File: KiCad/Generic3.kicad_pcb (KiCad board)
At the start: 2 copper layers, 35 x 21.5 mm, 35 parts, among them J1 DC, J2 I/O, J3 USB-C, U1 ESP32-PICO-MINI-02, U2 LMR16006+FB, U3 FT231XQ, U4 QR

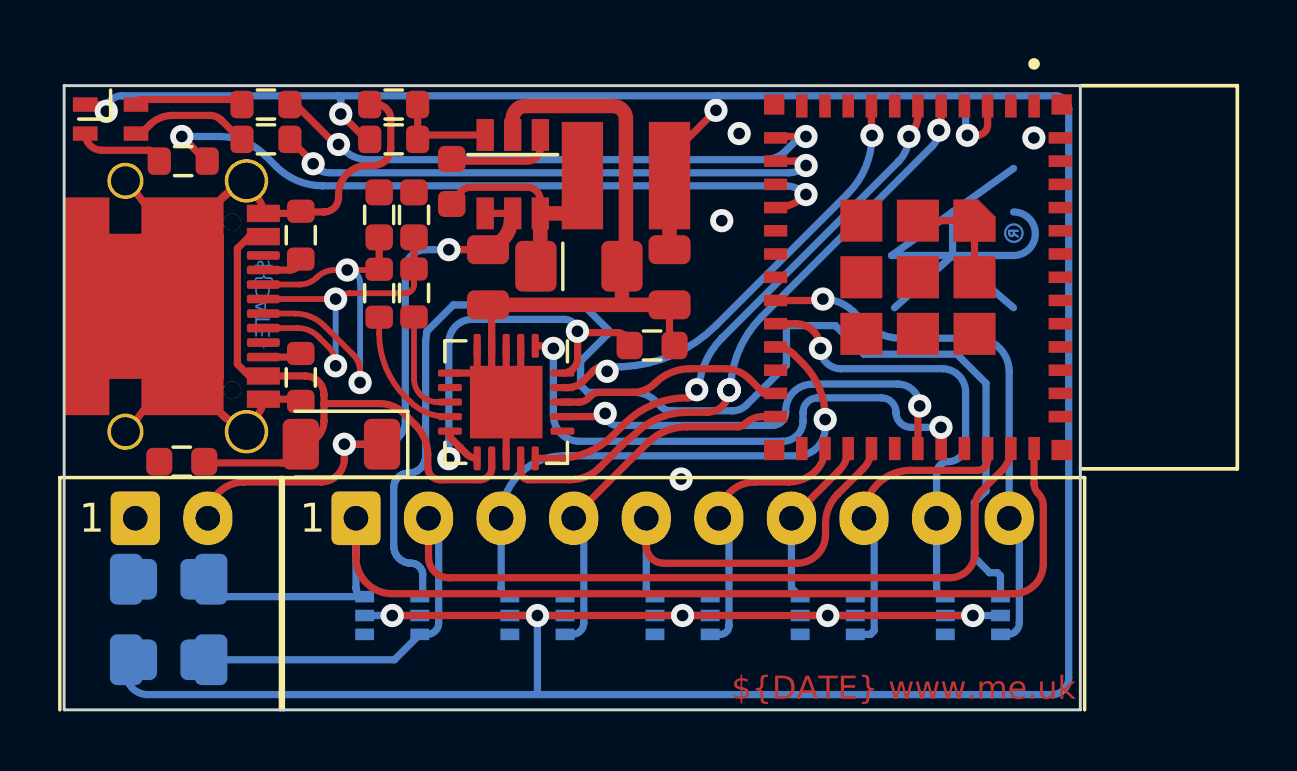
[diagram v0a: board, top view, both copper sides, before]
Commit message: Tidy GPIO usage
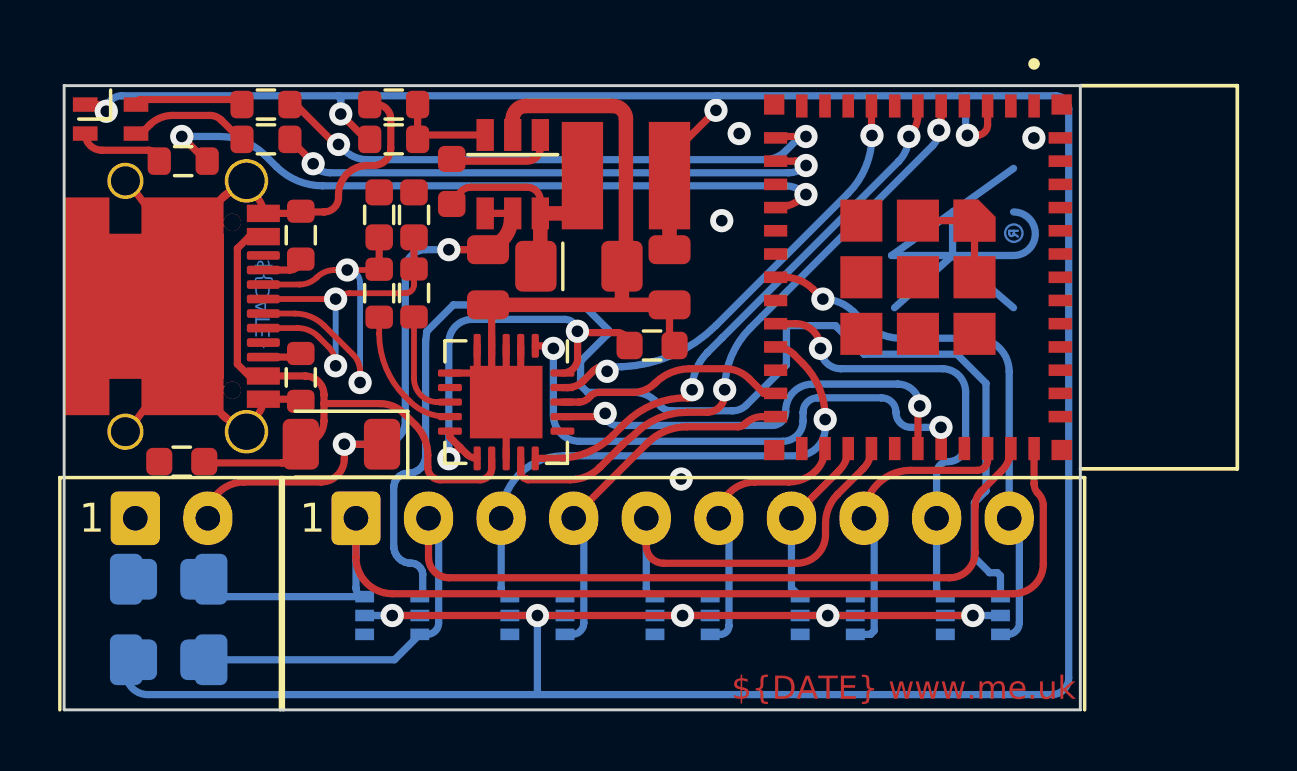
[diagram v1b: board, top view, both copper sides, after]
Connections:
- U1 pad 18: unconnected-(U1-Pad18) -> IO10
- U1 pad 19: IO10 -> unconnected-(U1-Pad19)
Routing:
- net CHARGER: vias 4 -> 2
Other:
- board text added: "14"
- board text removed: "12"
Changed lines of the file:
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@@
   (net 27 "CHARGER")
   (net 28 "USB")
-  (net 29 "unconnected-(U1-Pad18)")
+  (net 29 "unconnected-(U1-Pad19)")
   (net 30 "unconnected-(U1-Pad22)")
   (net 31 "GPIO0")
@@
       (primitives
     (gr_arc (start 2.89 -3.045) (mid 0 -0.155) (end -2.89 -3.045) (width 0.25))
-    (gr_arc (start 4.294753 -3.49127) (mid -0.020907 -1.02625) (end -4.315692 -3.527464) (width 0.25))
+    (gr_arc (start 4.294753 -3.49127) (mid -0.016568 -1.026234) (end -4.311371 -3.519937) (width 0.25))
     (gr_arc (start -3.2 -2.485) (mid -4.015 -3.3) (end -3.2 -4.115) (width 0.25))
     (gr_arc (start 3.2 -4.115) (mid 4.015 -3.3) (end 3.2 -2.485) (width 0.25))
-    (gr_arc (start -4.32 0.635) (mid 0 -1.154403) (end 4.32 0.635) (width 0.25))
+    (gr_arc (start -4.32 0.635) (mid -0.000001 -1.154403) (end 4.319999 0.634999) (width 0.25))
         (gr_poly (pts
             (xy -3.75 -2.745)
@@
       (net 44 "unconnected-(U1-Pad17)") (pinfunction "IO27") (pintype "bidirectional+no_connect"))
     (pad "18" smd rect (at 0 4.9 270) (size 0.4 0.8) (layers "F.Cu" "F.Paste" "F.Mask")
-      (net 29 "unconnected-(U1-Pad18)") (pinfunction "IO14") (pintype "bidirectional+no_connect"))
+      (net 14 "IO10") (pinfunction "IO14") (pintype "bidirectional"))
     (pad "19" smd rect (at 0.8 4.9 270) (size 0.4 0.8) (layers "F.Cu" "F.Paste" "F.Mask")
-      (net 14 "IO10") (pinfunction "IO12") (pintype "bidirectional"))
+      (net 29 "unconnected-(U1-Pad19)") (pinfunction "IO12") (pintype "bidirectional+no_connect"))
     (pad "20" smd rect (at 1.6 4.9 270) (size 0.4 0.8) (layers "F.Cu" "F.Paste" "F.Mask")
       (net 12 "IO9") (pinfunction "IO13") (pintype "bidirectional"))
@@
     (effects (font (size 1 1) (thickness 0.15)) (justify mirror))
   )
-  (gr_text "12" (at 169.5 74.75) (layer "B.SilkS")
+  (gr_text "14" (at 169.5 74.75) (layer "B.SilkS")
     (effects (font (size 1 1) (thickness 0.15)) (justify mirror))
   )
@@
   (arc (start 147.9 66.6) (mid 148.465685 66.365685) (end 148.7 65.8) (width 0.25) (layer "B.Cu") (net 13))
   (arc (start 148.7 60.6) (mid 148.905025 60.105025) (end 149.4 59.9) (width 0.25) (layer "B.Cu") (net 13))
-  (segment (start 161.45675 61.65) (end 162.963875 61.65) (width 0.25) (layer "F.Cu") (net 14))
+  (segment (start 162.741031 61.258969) (end 163.082801 61.600739) (width 0.25) (layer "F.Cu") (net 14))
+  (segment (start 161.45675 60.85) (end 161.753693 60.85) (width 0.25) (layer "F.Cu") (net 14))
   (via (at 163.082801 61.600739) (size 0.8) (drill 0.4) (layers "F.Cu" "B.Cu") (net 14))
-  (arc (start 162.963875 61.65) (mid 163.028237 61.637197) (end 163.082801 61.600739) (width 0.25) (layer "F.Cu") (net 14))
+  (arc (start 161.753693 60.85) (mid 162.288036 60.956288) (end 162.741031 61.258969) (width 0.25) (layer "F.Cu") (net 14))
   (segment (start 165.75 62.95) (end 168.35 62.95) (width 0.25) (layer "B.Cu") (net 14))
   (segment (start 169.5 64.1) (end 169.5 69.15) (width 0.25) (layer "B.Cu") (net 14))
@@
   (segment (start 167.096281 55.765112) (end 167.077425 55.783968) (width 0.25) (layer "F.Cu") (net 27))
   (segment (start 167.15675 54.95) (end 167.15675 55.628909) (width 0.25) (layer "F.Cu") (net 27))
+  (segment (start 159.7 64.724501) (end 159.7 64.895909) (width 0.25) (layer "F.Cu") (net 27))
   (segment (start 152.92452 67.82452) (end 154.375119 67.82452) (width 0.25) (layer "F.Cu") (net 27))
   (via (at 167.077425 55.783968) (size 0.8) (drill 0.4) (layers "F.Cu" "B.Cu") (net 27))
-  (via (at 159.848254 64.747655) (size 0.8) (drill 0.4) (layers "F.Cu" "B.Cu") (net 27))
-  (via (at 159.848254 64.747655) (size 0.8) (drill 0.4) (layers "F.Cu" "B.Cu") (net 27))
-  (via (at 159.858917 64.724501) (size 0.8) (drill 0.4) (layers "F.Cu" "B.Cu") (net 27))
-  (arc (start 159.095909 65.5) (mid 159.627897 65.279643) (end 159.848254 64.747655) (width 0.25) (layer "F.Cu") (net 27))
+  (via (at 159.7 64.724501) (size 0.8) (drill 0.4) (layers "F.Cu" "B.Cu") (net 27))
   (arc (start 156.180761 66.619239) (mid 156.375762 66.441302) (end 156.582369 66.276767) (width 0.25) (layer "F.Cu") (net 27))
+  (arc (start 159.7 64.895909) (mid 159.523066 65.323066) (end 159.095909 65.5) (width 0.25) (layer "F.Cu") (net 27))
   (arc (start 152.675 67.575) (mid 152.740901 67.734099) (end 152.9 67.8) (width 0.25) (layer "F.Cu") (net 27))
   (arc (start 154.375119 67.82452) (mid 154.929781 67.714191) (end 155.4 67.4) (width 0.25) (layer "F.Cu") (net 27))
   (arc (start 167.15675 55.628909) (mid 167.140248 55.694791) (end 167.096281 55.747573) (width 0.25) (layer "F.Cu") (net 27))
   (arc (start 156.623134 66.236002) (mid 157.438367 65.691281) (end 158.4 65.5) (width 0.25) (layer "F.Cu") (net 27))
-  (segment (start 159.937296 64.646122) (end 159.858917 64.724501) (width 0.25) (layer "B.Cu") (net 27))
   (segment (start 166.849668 56.333822) (end 160.972335 62.211156) (width 0.25) (layer "B.Cu") (net 27))
-  (segment (start 159.937296 64.262448) (end 159.937296 64.646122) (width 0.25) (layer "B.Cu") (net 27))
-  (arc (start 160.972335 62.211156) (mid 160.290925 63.153893) (end 159.937296 64.262448) (width 0.25) (layer "B.Cu") (net 27))
+  (segment (start 160.577527 62.605965) (end 160.972335 62.211156) (width 0.25) (layer "B.Cu") (net 27))
+  (arc (start 159.7 64.724501) (mid 159.928062 63.577957) (end 160.577527 62.605965) (width 0.25) (layer "B.Cu") (net 27))
   (arc (start 167.077425 55.783968) (mid 167.018233 56.081547) (end 166.849668 56.333822) (width 0.25) (layer "B.Cu") (net 27))
   (segment (start 156.262715 65.885293) (end 156.133426 66.014581) (width 0.25) (layer "F.Cu") (net 28))
   (segment (start 156.133426 66.014581) (end 155.848505 66.299502) (width 0.25) (layer "F.Cu") (net 28))
   (segment (start 166.35675 54.95) (end 166.35675 55.246475) (width 0.25) (layer "F.Cu") (net 28))
+  (segment (start 158.578424 64.7245) (end 158.578424 64.821576) (width 0.25) (layer "F.Cu") (net 28))
   (segment (start 153.94611 67.0875) (end 153.175 67.0875) (width 0.25) (layer "F.Cu") (net 28))
   (segment (start 158.461841 65) (end 158.4 65) (width 0.25) (layer "F.Cu") (net 28))
-  (via (at 158.737341 64.7245) (size 0.8) (drill 0.4) (layers "F.Cu" "B.Cu") (net 28))
+  (via (at 158.578424 64.7245) (size 0.8) (drill 0.4) (layers "F.Cu" "B.Cu") (net 28))
   (via (at 166.044629 56.000001) (size 0.8) (drill 0.4) (layers "F.Cu" "B.Cu") (net 28))
+  (arc (start 158.578424 64.821576) (mid 158.526165 64.947741) (end 158.4 65) (width 0.25) (layer "F.Cu") (net 28))
   (arc (start 155.848505 66.299502) (mid 154.975679 66.882706) (end 153.94611 67.0875) (width 0.25) (layer "F.Cu") (net 28))
   (arc (start 158.737341 64.7245) (mid 158.656649 64.919308) (end 158.461841 65) (width 0.25) (layer "F.Cu") (net 28))
   (arc (start 158.4 65) (mid 157.243309 65.23008) (end 156.262715 65.885293) (width 0.25) (layer "F.Cu") (net 28))
   (arc (start 166.35675 55.246475) (mid 166.275632 55.65428) (end 166.044629 56.000001) (width 0.25) (layer "F.Cu") (net 28))
-  (segment (start 158.836962 64.43365) (end 158.836962 64.624879) (width 0.25) (layer "B.Cu") (net 28))
-  (segment (start 158.836962 64.624879) (end 158.737341 64.7245) (width 0.25) (layer "B.Cu") (net 28))
   (segment (start 165.688847 56.858935) (end 159.614741 62.933041) (width 0.25) (layer "B.Cu") (net 28))
+  (segment (start 159.11239 63.435392) (end 159.614741 62.933041) (width 0.25) (layer "B.Cu") (net 28))
   (arc (start 166.044629 56.000001) (mid 165.952164 56.464853) (end 165.688847 56.858935) (width 0.25) (layer "B.Cu") (net 28))
-  (arc (start 159.614741 62.933041) (mid 159.11031 63.62325) (end 158.836962 64.43365) (width 0.25) (layer "B.Cu") (net 28))
+  (arc (start 158.578424 64.7245) (mid 158.717197 64.02684) (end 159.11239 63.435392) (width 0.25) (layer "B.Cu") (net 28))
   (segment (start 161.051934 64.85) (end 161.45675 64.85) (width 0.25) (layer "F.Cu") (net 31))
   (segment (start 160.550967 64.349033) (end 161.051934 64.85) (width 0.25) (layer "F.Cu") (net 31))

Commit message: Fixed USB/DC stuff on Generic.
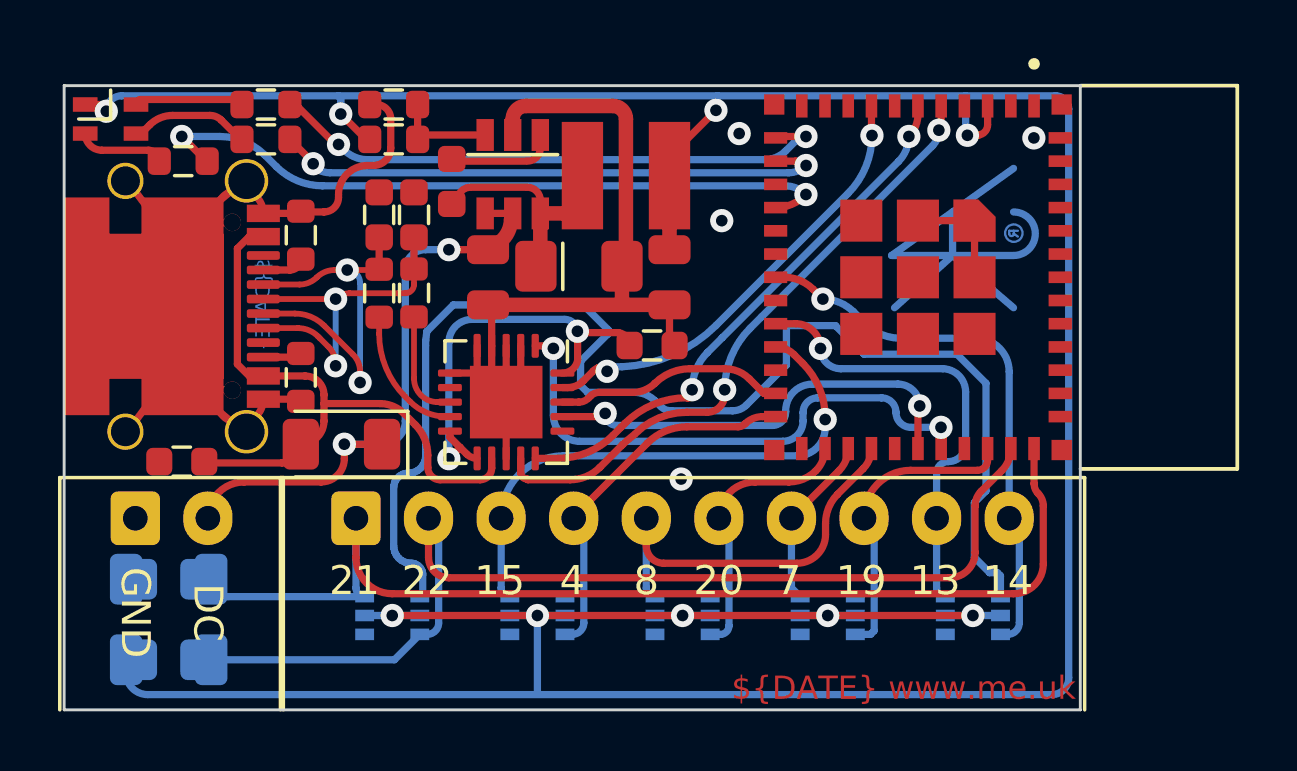
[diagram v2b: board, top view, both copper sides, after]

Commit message: Generic3 VBUS tidy
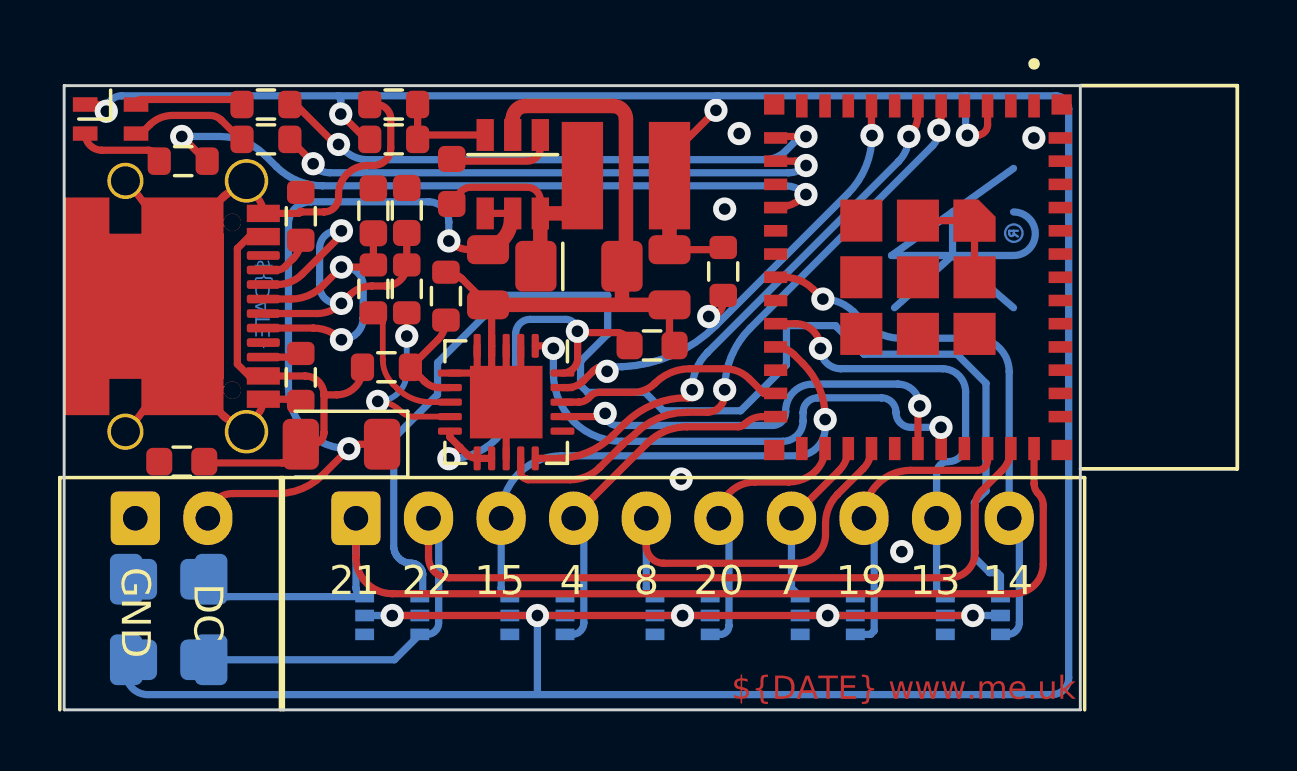
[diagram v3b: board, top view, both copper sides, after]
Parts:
- added R1: 10k, RevK:R_0603, F.Cu at (159.7, 60.6)
- added R11: 4k7, RevK:R_0603, F.Cu at (148.1, 64.0)
- added R12: 10k, RevK:R_0603, F.Cu at (150.1, 61.5)
- moved C3 1.41 mm to (147.6, 58.6)
- moved R8 1.41 mm to (147.6, 61.2)
- moved C1 0.96 mm to (148.8, 58.5)
- moved R7 0.96 mm to (148.8, 61.2)
- moved R5 0.65 mm to (145.1, 58.8)
- renumbered C4 to C2, C2 to C3, C3 to C4, R9 to R10, R1 to R2, R2 to R3, R3 to R4, R4 to R5, R5 to R6, R6 to R7, R7 to R8, R8 to R9, U3 to U2, U2 to U3
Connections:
- C2 pad 1: Net-(C4-Pad1) -> Net-(C2-Pad1)
- U2 pad 10: Net-(C4-Pad1) -> Net-(C2-Pad1)
- U2 pad 11: Net-(C4-Pad1) -> Net-(C2-Pad1)
- U2 pad 12: VBUS -> Net-(C2-Pad1)
- U2 pad 20: Net-(C4-Pad1) -> Net-(C2-Pad1)
- U2 pad 7: unconnected-(U3-Pad7) -> Net-(R11-Pad2)
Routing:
- net Net-(C4-Pad1): track 14.8 -> 0.00 mm, vias 2 -> 0
- net Net-(C2-Pad1): track 0.00 -> 14.4 mm, vias 0 -> 2
- net VBUS: track 22.3 -> 16.4 mm
- net DC: track 19.5 -> 25.2 mm
- net Net-(R11-Pad2): track 0.00 -> 3.70 mm
- net GND: track 71.3 -> 73.3 mm, vias 4 -> 5
- net +3V3: track 128.3 -> 130.2 mm
- net D-: track 4.70 -> 6.20 mm, vias 0 -> 2
- net EN: track 15.7 -> 17.1 mm, vias 2 -> 3
- net D+: track 3.79 -> 4.86 mm
- net Net-(C3-Pad1): track 12.5 -> 11.4 mm
- net O: track 19.0 -> 18.3 mm

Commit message: Clean up GPIOs used to avoid clash with strapping at startup
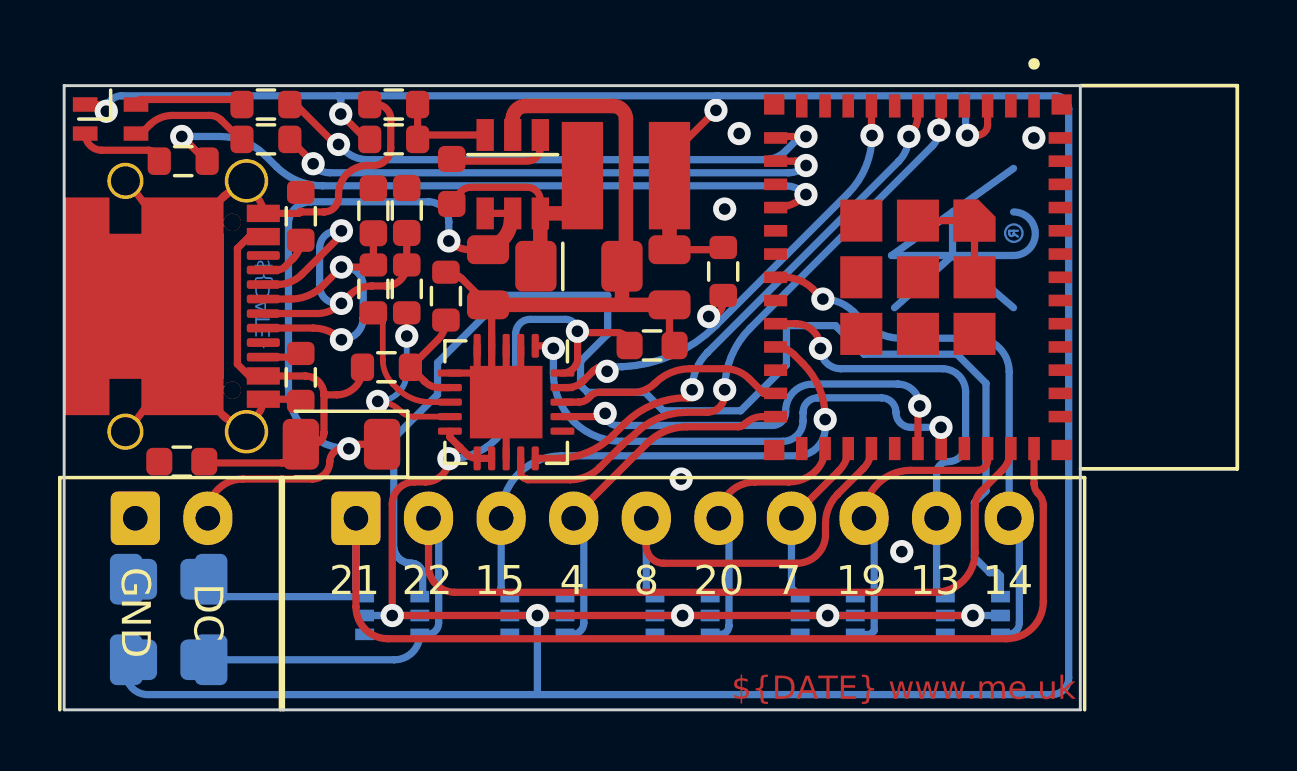
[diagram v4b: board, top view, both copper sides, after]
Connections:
- C2 pad 1: Net-(C2-Pad1) -> +3V3
- U2 pad 10: Net-(C2-Pad1) -> +3V3
- U2 pad 11: Net-(C2-Pad1) -> +3V3
- U2 pad 12: Net-(C2-Pad1) -> +3V3
- U2 pad 20: Net-(C2-Pad1) -> +3V3
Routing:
- net +3V3: track 130.2 -> 151.1 mm, vias 9 -> 11
- net Net-(C2-Pad1): track 14.4 -> 0.00 mm, vias 2 -> 0
- net IO1: track 39.4 -> 42.4 mm
- net IO2: track 37.2 -> 37.9 mm

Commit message: Footprint update
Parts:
- U2: footprint Package_DFN_QFN:QFN-20-1EP_4x4mm_P0.5mm_EP2.5x2.5mm -> RevK:QFN-20-1EP_4x4mm_P0.5mm_EP2.5x2.5mm
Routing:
- net GND: track 73.3 -> 69.4 mm
